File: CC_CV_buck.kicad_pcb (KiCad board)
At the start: 4 copper layers, 115.9 x 39 mm, 76 parts, among them J5 Conn_01x02_Pin, J6 Conn_01x02_Pin, J7 Conn_01x02_Pin, J8 Conn_01x02_Pin, Q1 TIP42C, Q2 AO3400A, Q3 MMBT3906, Q4 MMBT3904, U1 OPA2197xD, U2 INA194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

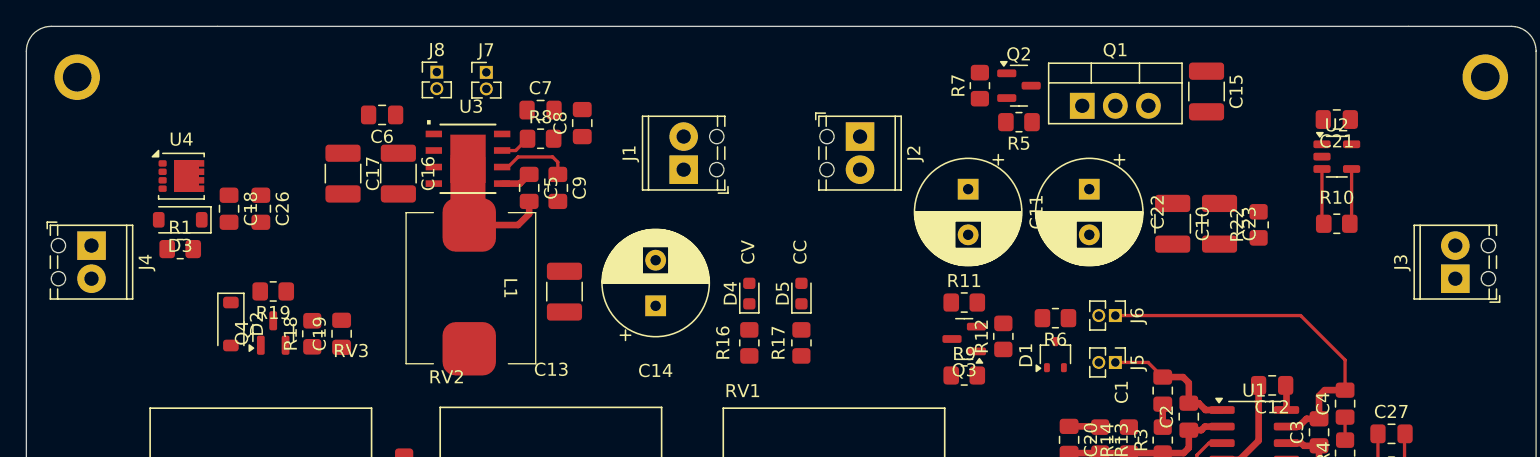
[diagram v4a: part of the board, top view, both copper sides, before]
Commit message: do a bunch of polygon pours
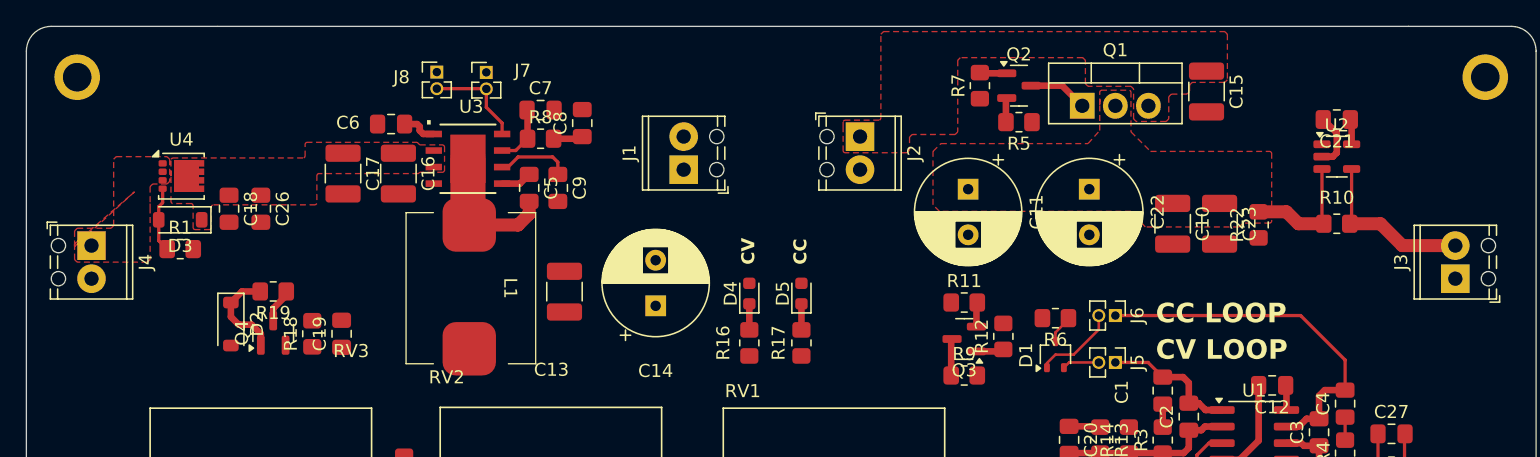
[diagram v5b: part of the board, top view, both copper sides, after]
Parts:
- moved C6 0.98 mm to (79.0, 76.5)
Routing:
- net VOUT_LDO: track 6.67 -> 15.5 mm
- net /BUCK_FB: track 0.00 -> 7.77 mm
- net Net-(D2-K): track 0.00 -> 7.42 mm
- net Net-(J6-Pin_2): track 0.00 -> 6.47 mm
- net Net-(Q1-C): track 4.26 -> 9.64 mm
- net Net-(D3-A): track 0.00 -> 5.03 mm
- net Net-(Q1-B): track 0.00 -> 4.56 mm
- net GND: track 7.66 -> 11.9 mm
- net Net-(J5-Pin_2): track 0.00 -> 2.85 mm
- net Net-(J7-Pin_1): track 0.09 -> 2.83 mm
- net /BUCK_SS: track 0.00 -> 2.73 mm
- net P13V0: track 0.00 -> 2.66 mm
- net Net-(C8-Pad1): track 0.00 -> 2.27 mm
- net /BUCK_COMP: track 2.33 -> 4.54 mm
- net Net-(D1-Pad3): track 0.00 -> 2.21 mm
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- added copper zone on F.Cu, net Net-(Q1-C)
- added copper zone on F.Cu, net P13V0
- added copper zone on F.Cu, net VIN
- added copper zone on F.Cu, net VIN_LDO
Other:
- board text added: "CC LOOP"
- board text added: "CV LOOP"

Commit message: editing some polygons
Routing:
- added copper zone on F.Cu, net VOUT_BUCK
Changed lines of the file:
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@@
 		(polygon
 			(pts
-				(xy 62.1 80.5) (xy 62.1 80.5) (xy 62.1 79.2) (xy 62.2 79.1) (xy 72.3 79.1) (xy 72.4 79) (xy 72.4 78)
-				(xy 72.5 77.9) (xy 81 77.9) (xy 81.2 78.1) (xy 83 78.1) (xy 83.1 78.2) (xy 83.1 80.1) (xy 83 80.2)
-				(xy 81.2 80.2) (xy 81.1 80.3) (xy 73.4 80.3) (xy 73.3 80.4) (xy 73.3 82.6) (xy 73.2 82.7) (xy 65.3 82.7)
-				(xy 65.2 82.8) (xy 65.2 84.5) (xy 65.1 84.6) (xy 63.9 84.6) (xy 63.8 84.5) (xy 63.8 82.7) (xy 63.7 82.6)
-				(xy 62.2 82.6) (xy 62.1 82.5) (xy 62.1 80.1)
+				(xy 62.1 80.5) (xy 62.1 79.2) (xy 62.2 79.1) (xy 72.3 79.1) (xy 72.4 79) (xy 72.4 78) (xy 72.5 77.9)
+				(xy 81 77.9) (xy 81.2 78.1) (xy 83 78.1) (xy 83.1 78.2) (xy 83.1 80.1) (xy 83 80.2) (xy 81.2 80.2)
+				(xy 81.1 80.3) (xy 73.4 80.3) (xy 73.3 80.4) (xy 73.3 82.6) (xy 73.2 82.7) (xy 65.3 82.7) (xy 65.2 82.8)
+				(xy 65.2 84.5) (xy 65.1 84.6) (xy 63.9 84.6) (xy 63.8 84.5) (xy 63.8 82.7) (xy 63.7 82.6) (xy 62.2 82.6)
+				(xy 62.1 82.5) (xy 62.1 80.1)
 			)
 		)
@@
 		(polygon
 			(pts
-				(xy 133.4 74.7) (xy 133.4 75) (xy 133.4 74) (xy 133.5 73.9) (xy 135.7 73.9) (xy 135.8 74) (xy 135.8 77.1)
-				(xy 137.3 78.6) (xy 146.5 78.6) (xy 146.6 78.7) (xy 146.6 84) (xy 146.5 84.1) (xy 144.4 84.1) (xy 144.1 84.4)
-				(xy 136.9 84.4) (xy 135.8 83.2) (xy 121.1 83.2) (xy 120.6 82.7) (xy 120.6 78.6) (xy 121.2 78) (xy 132.5 78)
-				(xy 133.4 77) (xy 133.4 74.6)
+				(xy 133.4 74.7) (xy 133.4 75) (xy 133.4 74) (xy 133.5 73.9) (xy 135.7 73.9) (xy 135.8 74) (xy 135.8 77.6)
+				(xy 136.2 78) (xy 146.1 78) (xy 146.6 78.4) (xy 146.6 84) (xy 146.5 84.1) (xy 144.4 84.1) (xy 144.1 84.4)
+				(xy 136.9 84.4) (xy 135.8 83.2) (xy 121.1 83.2) (xy 120.6 82.7) (xy 120.6 78.6) (xy 121.2 78) (xy 133 78)
+				(xy 133.4 77.6) (xy 133.4 74.6)
 			)
 		)
+	)
+	(zone
+		(net 8)
+		(net_name "VOUT_BUCK")
+		(layer "F.Cu")
+		(hatch edge 0.5)
+		(priority 2)
+		(connect_pads yes
+			(clearance 0.2)
+		)
+		(min_thickness 0.2)
+		(filled_areas_thickness no)
+		(fill yes
+			(thermal_gap 0.5)
+			(thermal_bridge_width 0.5)
+			(island_removal_mode 1)
+			(island_area_min 10)
+		)
+		(polygon
+			(pts
+				(xy 82.7 91.7) (xy 82.9 91.5) (xy 90.6 91.5) (xy 90.8 91.3) (xy 90.8 90.3) (xy 91 90.1) (xy 98 90.1)
+				(xy 98.2 89.9) (xy 98.2 89.1) (xy 98.4 88.9) (xy 100.1 88.9) (xy 100.3 88.7) (xy 100.3 79) (xy 100.5 78.8)
+				(xy 102.4 78.8) (xy 102.9 79.3) (xy 102.9 95.8) (xy 102.7 96) (xy 83 96) (xy 82.8 95.8) (xy 82.7 95.7)
+				(xy 82.7 92.8)
+			)
+		)

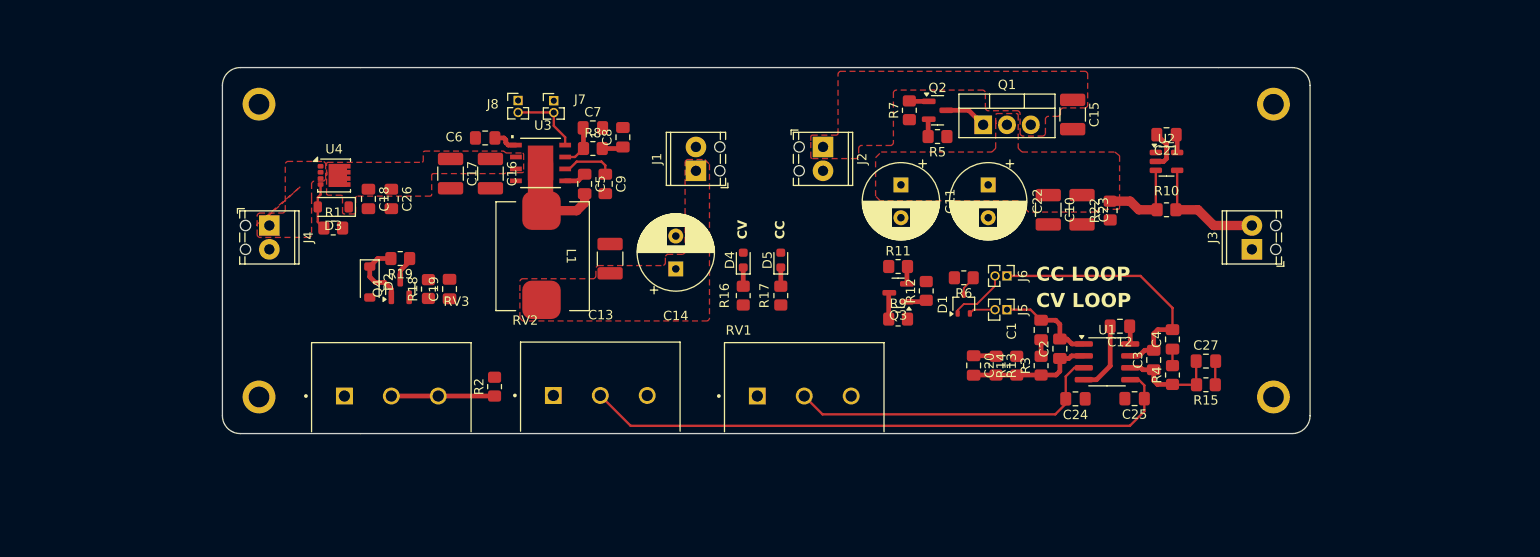
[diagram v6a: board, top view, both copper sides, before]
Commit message: change regulator and finish layout
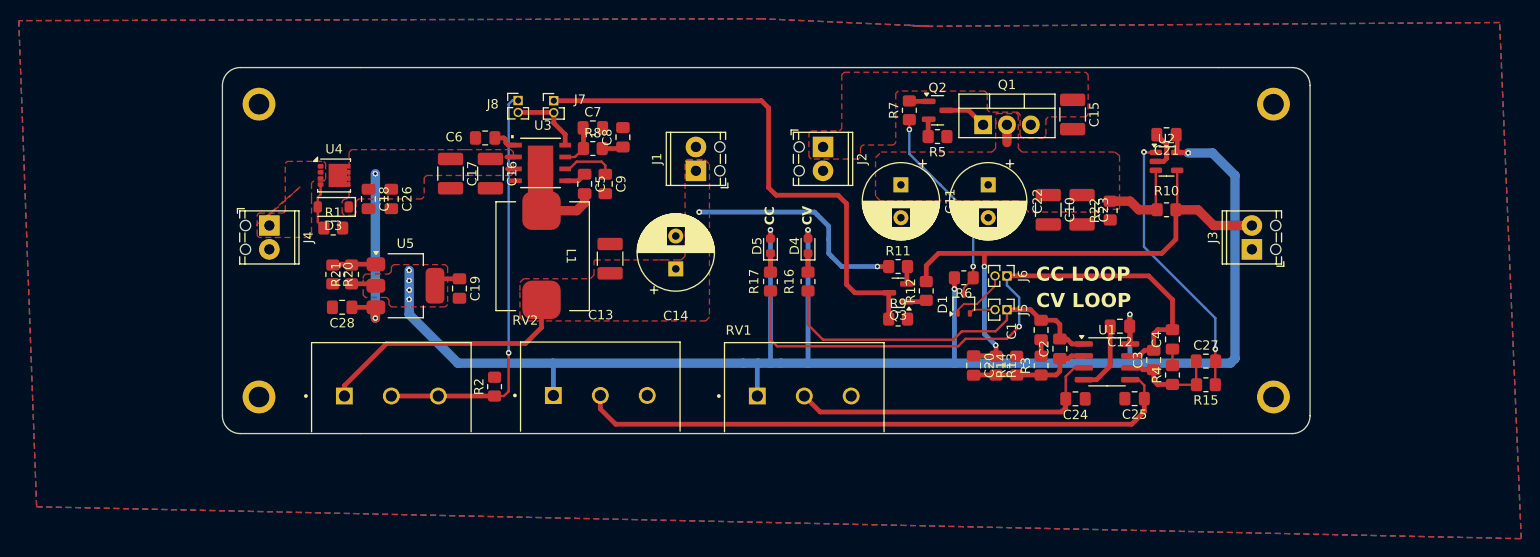
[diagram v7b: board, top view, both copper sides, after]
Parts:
- removed D2: MMSZ5240BT1G, Diode_SMD:D_SOD-123
- removed Q4: MMBT3904, Package_TO_SOT_SMD:SOT-23
- removed R18: 1k, Resistor_SMD:R_0805_2012Metric_Pad1.20x1.40mm_HandSolder
- removed R19: 330, Resistor_SMD:R_0805_2012Metric_Pad1.20x1.40mm_HandSolder
- added C28: 100n, Capacitor_SMD:C_0805_2012Metric_Pad1.18x1.45mm_HandSolder, F.Cu at (63.8, 94.5)
- added R20: 6k8, Resistor_SMD:R_0805_2012Metric_Pad1.20x1.40mm_HandSolder, F.Cu at (62.8, 91.0)
- added R21: 1k, Resistor_SMD:R_0805_2012Metric_Pad1.20x1.40mm_HandSolder, F.Cu at (64.8, 91.0)
- added U5: LM317_SOT-223, Package_TO_SOT_SMD:SOT-223-3_TabPin2, F.Cu at (70.5, 92.2)
- moved D4 7.06 mm to (113.4, 88.0)
- moved R16 7.06 mm to (113.4, 91.8)
- moved D5 1.86 mm to (109.4, 88.0)
- moved R17 1.86 mm to (109.4, 91.8)
- moved C19 1.06 mm to (76.3, 92.5), turned to -90 degrees
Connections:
- net P13V0 renamed VIN_P
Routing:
- net Vcc: track 3.86 -> 184.0 mm, vias 0 -> 9
- net Net-(J7-Pin_1): track 2.83 -> 57.1 mm
- net VOUT_BUCK: track 0.00 -> 51.9 mm, vias 0 -> 2
- net VOUT_LDO: track 15.5 -> 59.5 mm, vias 0 -> 2
- net /CC_out: track 28.1 -> 67.4 mm, vias 0 -> 1
- net Net-(J8-Pin_1): track 11.0 -> 44.5 mm, vias 0 -> 1
- net /CV_out: track 10.7 -> 38.0 mm
- net /I_SNS: track 2.53 -> 29.3 mm, vias 0 -> 2
- net Net-(D1-Pad3): track 2.21 -> 21.9 mm, vias 0 -> 2
- net VIN_P: track 2.66 -> 21.7 mm, vias 0 -> 2
- net Net-(D2-K): track 7.42 -> 0.00 mm
- net Net-(U5-ADJ): track 0.00 -> 4.63 mm
- net Net-(Q1-C): track 9.64 -> 11.5 mm
- net /ISET: track 64.5 -> 65.2 mm
- added copper zone on B.Cu, net GND
- added copper zone on F.Cu, net GND
- added copper zone on In1.Cu, net GND
- added copper zone on F.Cu, net Vcc

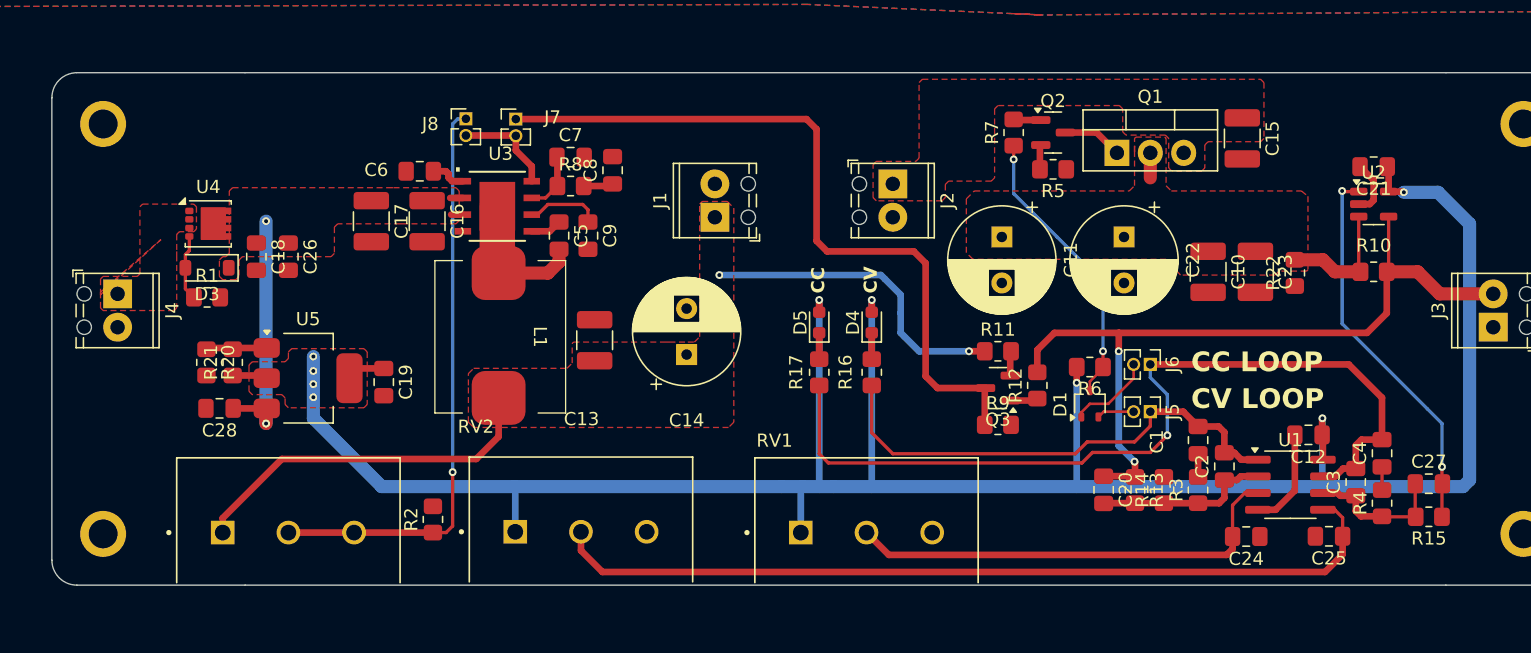
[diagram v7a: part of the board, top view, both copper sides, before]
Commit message: clean silkscreen and refdes
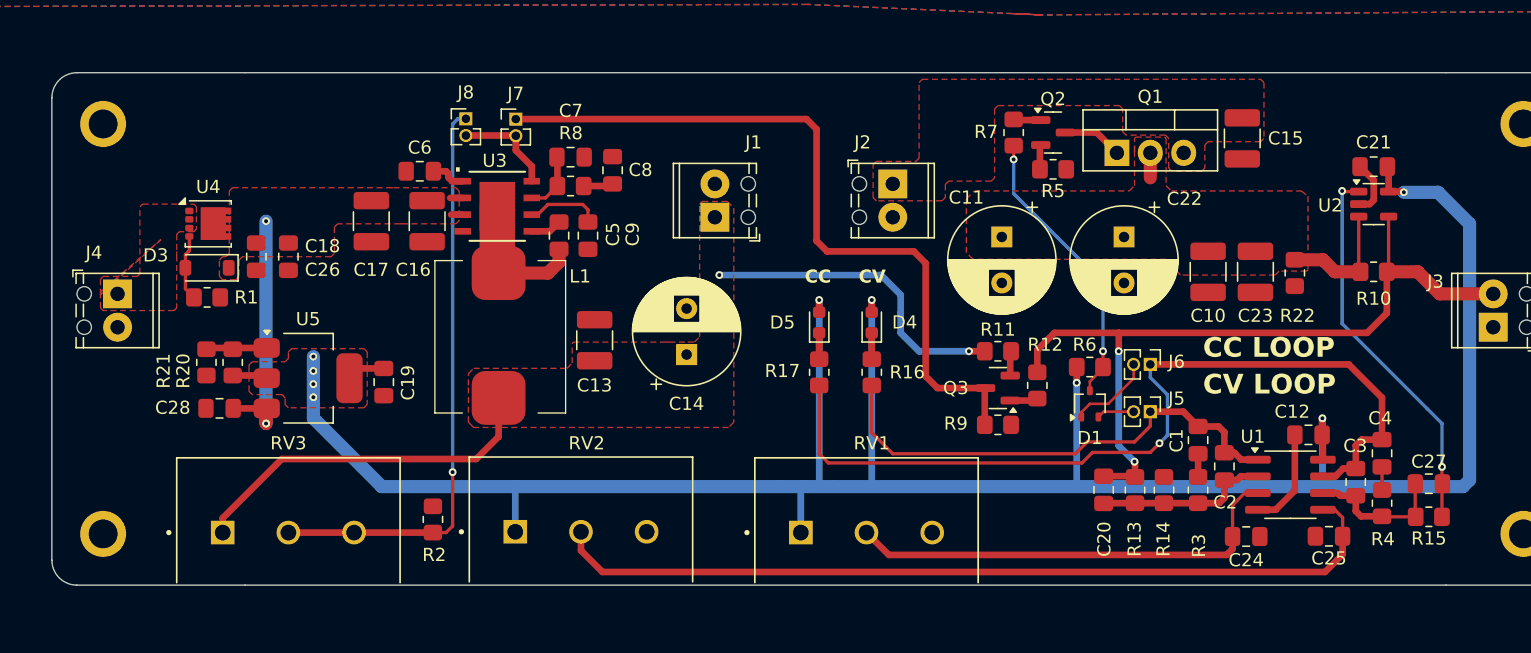
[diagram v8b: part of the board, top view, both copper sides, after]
